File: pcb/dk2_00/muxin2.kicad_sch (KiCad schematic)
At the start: 7 parts, among them J12 AudioJack2_SwitchT, U15 MCP6002-xSN, U6 74HC4051

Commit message: tidying up, getting close!
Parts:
- added C23: 1n, symbol Device:C_Polarized_US
- added J12: AudioJack2_SwitchT, AudioJacks:Jack_3.5mm_QingPu_WQP-PJ398SM_Vertical, symbol Connector_Audio:AudioJack2_SwitchT
- added J9: Conn_01x08_Pin, symbol Connector:Conn_01x08_Pin
- added R32: 240k, symbol Device:R_US
- added R33: 100k, symbol Device:R_US
- added R35: 33k, symbol Device:R_US
- renumbered C27 to C22, R49 to R30, R48 to R31, R50 to R34
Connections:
- net +3V3 is gone; now on net +3.3V: U6.16 (VCC)
- net -12V: now also R30.1, R32.1
- net GND: now also J12.S, U15.3 (+), U15.4 (V-), U15.5 (+), J12.S, J9.8 (Pin_8)
- net at C22.1: now also R30.2, R31.2, R34.1, U15.2 (-)
- net CV_IN_1: now reaches C22.2
- net CV_IN_1: now also R34.2, U15.1, U6.13 (A0)
- net at U15.6 (-): now also C23.1, R32.2, R33.2, R35.1
- net CV_IN_2: now reaches U15.7
- net CV_IN_2: now also U6.14 (A1), C23.2, R35.2
- net +3.3V: now reaches U15.8 (V+)
- net +3.3V: now also J9.1 (Pin_1)
- net at U6.1 (A4): now also J9.4 (Pin_4)
- net at U6.12 (A3): now also J9.3 (Pin_3)
- net at U6.15 (A2): now also J9.2 (Pin_2)
- net at U6.2 (A6): now also J9.6 (Pin_6)
- net at U6.4 (A7): now also J9.7 (Pin_7)
- net at U6.5 (A5): now also J9.5 (Pin_5)
- new net: J12.T, R33.1
- no-connect marks 2 -> 3
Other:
- moved on the sheet: C22, R34, U15B, U15C

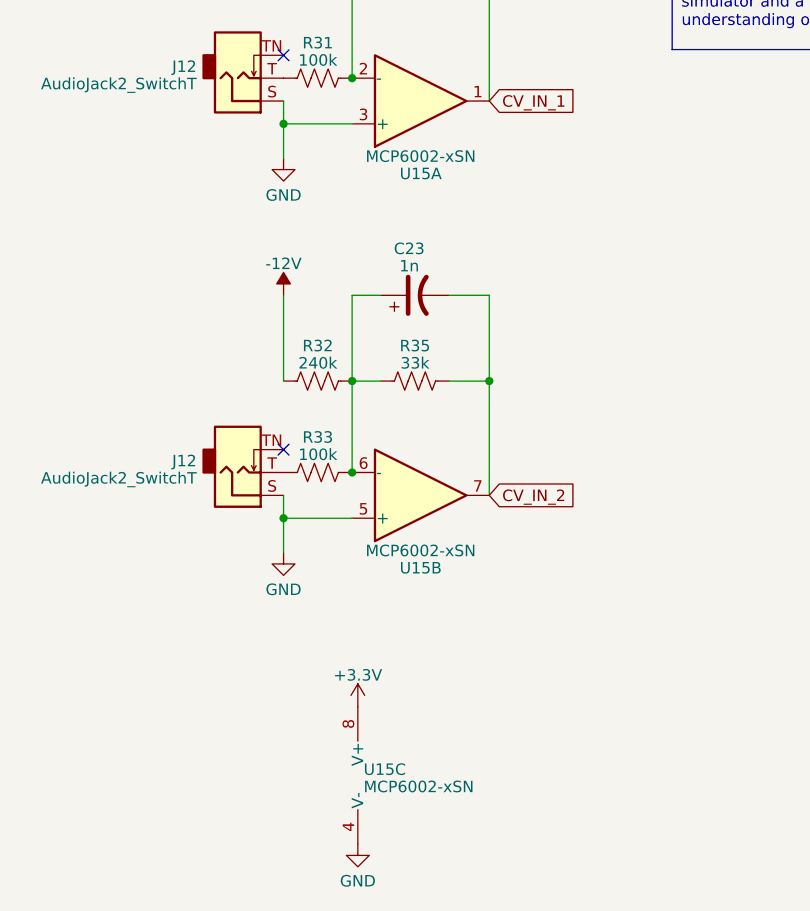
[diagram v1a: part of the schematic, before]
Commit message: barrel jack, power pins
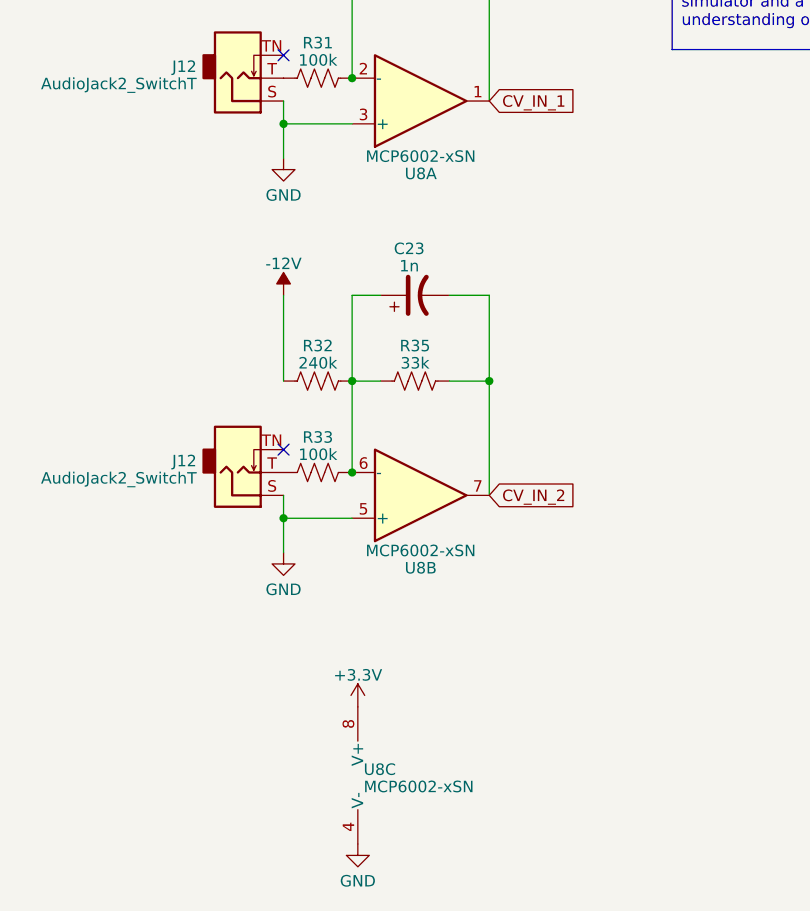
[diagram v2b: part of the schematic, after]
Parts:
- renumbered U15 to U8
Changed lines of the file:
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@@
   (symbol (lib_id "Amplifier_Operational:MCP6002-xSN") (at 83.185 48.895 0) (mirror x) (unit 1)
     (in_bom yes) (on_board yes) (dnp no)
-    (property "Reference" "U15" (at 83.185 56.9849 0)
+    (property "Reference" "U8" (at 83.185 56.9849 0)
       (effects (font (size 1.27 1.27)))
     )
@@
   (symbol (lib_id "Amplifier_Operational:MCP6002-xSN") (at 83.185 92.71 0) (mirror x) (unit 2)
     (in_bom yes) (on_board yes) (dnp no)
-    (property "Reference" "U15" (at 83.185 100.7999 0)
+    (property "Reference" "U8" (at 83.185 100.7999 0)
       (effects (font (size 1.27 1.27)))
     )
@@
   (symbol (lib_id "Amplifier_Operational:MCP6002-xSN") (at 78.74 123.825 0) (unit 3)
     (in_bom yes) (on_board yes) (dnp no) (fields_autoplaced)
-    (property "Reference" "U15" (at 76.835 123.1813 0)
+    (property "Reference" "U8" (at 76.835 123.1813 0)
       (effects (font (size 1.27 1.27)) (justify left))
     )

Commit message: components...
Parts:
- C22, C23: footprint (none) -> Capacitor_SMD:C_0603_1608Metric
- J9: footprint (none) -> Connector_PinHeader_2.54mm:PinHeader_1x08_P2.54mm_Vertical
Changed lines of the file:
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@@
       (effects (font (size 1.27 1.27)))
     )
-    (property "Footprint" "" (at 82.55 26.67 0)
+    (property "Footprint" "Capacitor_SMD:C_0603_1608Metric" (at 82.55 26.67 0)
       (effects (font (size 1.27 1.27)) hide)
     )
@@
       (effects (font (size 1.27 1.27)))
     )
-    (property "Footprint" "" (at 82.55 70.485 0)
+    (property "Footprint" "Capacitor_SMD:C_0603_1608Metric" (at 82.55 70.485 0)
       (effects (font (size 1.27 1.27)) hide)
     )
@@
       (effects (font (size 1.27 1.27)) (justify right))
     )
-    (property "Footprint" "" (at 201.93 98.425 0)
-      (effects (font (size 1.27 1.27)) hide)
-    )
+    (property "Footprint" "Connector_PinHeader_2.54mm:PinHeader_1x08_P2.54mm_Vertical" (at 201.93 98.425 0)
+      (effects (font (size 1.27 1.27)) hide)
+    )

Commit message: footprints assigned
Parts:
- R30, R31, R32, R33, R34, R35: footprint (none) -> Resistor_SMD:R_0603_1608Metric
- U8: footprint (none) -> Package_SO:SOIC-8_3.9x4.9mm_P1.27mm
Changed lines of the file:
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@@
       (effects (font (size 1.27 1.27)))
     )
-    (property "Footprint" "" (at 72.009 78.994 90)
+    (property "Footprint" "Resistor_SMD:R_0603_1608Metric" (at 72.009 78.994 90)
       (effects (font (size 1.27 1.27)) hide)
     )
@@
       (effects (font (size 1.27 1.27)))
     )
-    (property "Footprint" "" (at 83.185 48.895 0)
+    (property "Footprint" "Package_SO:SOIC-8_3.9x4.9mm_P1.27mm" (at 83.185 48.895 0)
       (effects (font (size 1.27 1.27)) hide)
     )
@@
       (effects (font (size 1.27 1.27)))
     )
-    (property "Footprint" "" (at 82.804 78.994 90)
+    (property "Footprint" "Resistor_SMD:R_0603_1608Metric" (at 82.804 78.994 90)
       (effects (font (size 1.27 1.27)) hide)
     )
@@
       (effects (font (size 1.27 1.27)))
     )
-    (property "Footprint" "" (at 83.185 92.71 0)
+    (property "Footprint" "Package_SO:SOIC-8_3.9x4.9mm_P1.27mm" (at 83.185 92.71 0)
       (effects (font (size 1.27 1.27)) hide)
     )
@@
       (effects (font (size 1.27 1.27)))
     )
-    (property "Footprint" "" (at 72.009 35.179 90)
+    (property "Footprint" "Resistor_SMD:R_0603_1608Metric" (at 72.009 35.179 90)
       (effects (font (size 1.27 1.27)) hide)
     )
@@
       (effects (font (size 1.27 1.27)) (justify left))
     )
-    (property "Footprint" "" (at 78.74 123.825 0)
+    (property "Footprint" "Package_SO:SOIC-8_3.9x4.9mm_P1.27mm" (at 78.74 123.825 0)
       (effects (font (size 1.27 1.27)) hide)
     )
@@
       (effects (font (size 1.27 1.27)))
     )
-    (property "Footprint" "" (at 72.009 45.339 90)
+    (property "Footprint" "Resistor_SMD:R_0603_1608Metric" (at 72.009 45.339 90)
       (effects (font (size 1.27 1.27)) hide)
     )
@@
       (effects (font (size 1.27 1.27)))
     )
-    (property "Footprint" "" (at 72.009 89.154 90)
+    (property "Footprint" "Resistor_SMD:R_0603_1608Metric" (at 72.009 89.154 90)
       (effects (font (size 1.27 1.27)) hide)
     )
@@
       (effects (font (size 1.27 1.27)))
     )
-    (property "Footprint" "" (at 82.804 35.179 90)
-      (effects (font (size 1.27 1.27)) hide)
-    )
+    (property "Footprint" "Resistor_SMD:R_0603_1608Metric" (at 82.804 35.179 90)
+      (effects (font (size 1.27 1.27)) hide)
+    )

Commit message: this layout is complicated!
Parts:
- J12: value AudioJack2_SwitchT -> CV_In_2
- J12: value AudioJack2_SwitchT -> CV_In_1
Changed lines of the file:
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@@
   (symbol (lib_id "Connector_Audio:AudioJack2_SwitchT") (at 62.865 90.17 0) (mirror x) (unit 1)
     (in_bom yes) (on_board yes) (dnp no) (fields_autoplaced)
-    (property "Reference" "J12" (at 58.293 88.8913 0)
+    (property "Reference" "J12" (at 57.15 88.9 0)
       (effects (font (size 1.27 1.27)) (justify right))
     )
-    (property "Value" "AudioJack2_SwitchT" (at 58.293 90.8123 0)
+    (property "Value" "CV_In_2" (at 57.15 91.44 0)
       (effects (font (size 1.27 1.27)) (justify right))
     )
@@
   (symbol (lib_id "Connector_Audio:AudioJack2_SwitchT") (at 62.865 46.355 0) (mirror x) (unit 1)
     (in_bom yes) (on_board yes) (dnp no) (fields_autoplaced)
-    (property "Reference" "J12" (at 58.293 45.0763 0)
+    (property "Reference" "J12" (at 57.15 45.085 0)
       (effects (font (size 1.27 1.27)) (justify right))
     )
-    (property "Value" "AudioJack2_SwitchT" (at 58.293 46.9973 0)
+    (property "Value" "CV_In_1" (at 57.15 47.625 0)
       (effects (font (size 1.27 1.27)) (justify right))
     )

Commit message: it's jlc time
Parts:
- J12: footprint AudioJacks:Jack_3.5mm_QingPu_WQP-PJ398SM_Vertical -> Library:Jack_3.5mm_QingPu_WQP-PJ398SM_Vertical_Labelled
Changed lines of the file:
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@@
       (effects (font (size 1.27 1.27)) (justify right))
     )
-    (property "Footprint" "AudioJacks:Jack_3.5mm_QingPu_WQP-PJ398SM_Vertical" (at 62.865 90.17 0)
+    (property "Footprint" "Library:Jack_3.5mm_QingPu_WQP-PJ398SM_Vertical_Labelled" (at 62.865 90.17 0)
       (effects (font (size 1.27 1.27)) hide)
     )
@@
       (effects (font (size 1.27 1.27)) (justify right))
     )
-    (property "Footprint" "AudioJacks:Jack_3.5mm_QingPu_WQP-PJ398SM_Vertical" (at 62.865 46.355 0)
+    (property "Footprint" "Library:Jack_3.5mm_QingPu_WQP-PJ398SM_Vertical_Labelled" (at 62.865 46.355 0)
       (effects (font (size 1.27 1.27)) hide)
     )
